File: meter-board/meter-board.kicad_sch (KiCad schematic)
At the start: 0 parts

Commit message: add title, revision
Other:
- title: (none) -> FET-PCB-meter
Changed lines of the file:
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@@
 	(generator_version "9.0")
 	(paper "A4")
+	(title_block
+		(title "FET-PCB-meter")
+		(rev "v1.0")
+	)
 	(sheet_instances
 		(path "/"

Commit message: add protection circuit
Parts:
- added D1: DF2B36FU,H3F, my_Protection:DF2B36FU,H3F, symbol my_Protection:DF2B36FU,H3F
- added D2: MM3Z12VST1G, my_Diode:MM3Z12VST1G, symbol my_Diode:MM3Z12VST1G
- added F1: 0686F0500-01, my_Fuse:0686F0500-01, symbol my_Fuse:0686F0500-01
- added J1: 2-1445053-2, my_Connector:2-1445053-2, symbol my_Connector:2-1445053-2
- added Q1: PMN100EPAX, my_Transistor:PMN100EPAX, symbol my_Transistor:PMN100EPAX
- added R1: R, my_Resistor:R_0402_1005M, symbol my_Resistor:R_0402_1005M
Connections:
- new net: F1.1, J1.1 (Pin_1)
- new net: D1.2 (A2), J1.2 (Pin_2), R1.1
- new net: D2.1 (K), Q1.4 (S)
- new net: D2.2 (A), Q1.3 (G), R1.2
- new net: D1.1 (A1), F1.2, Q1.1 (D), Q1.2 (D), Q1.5 (D), Q1.6 (D)

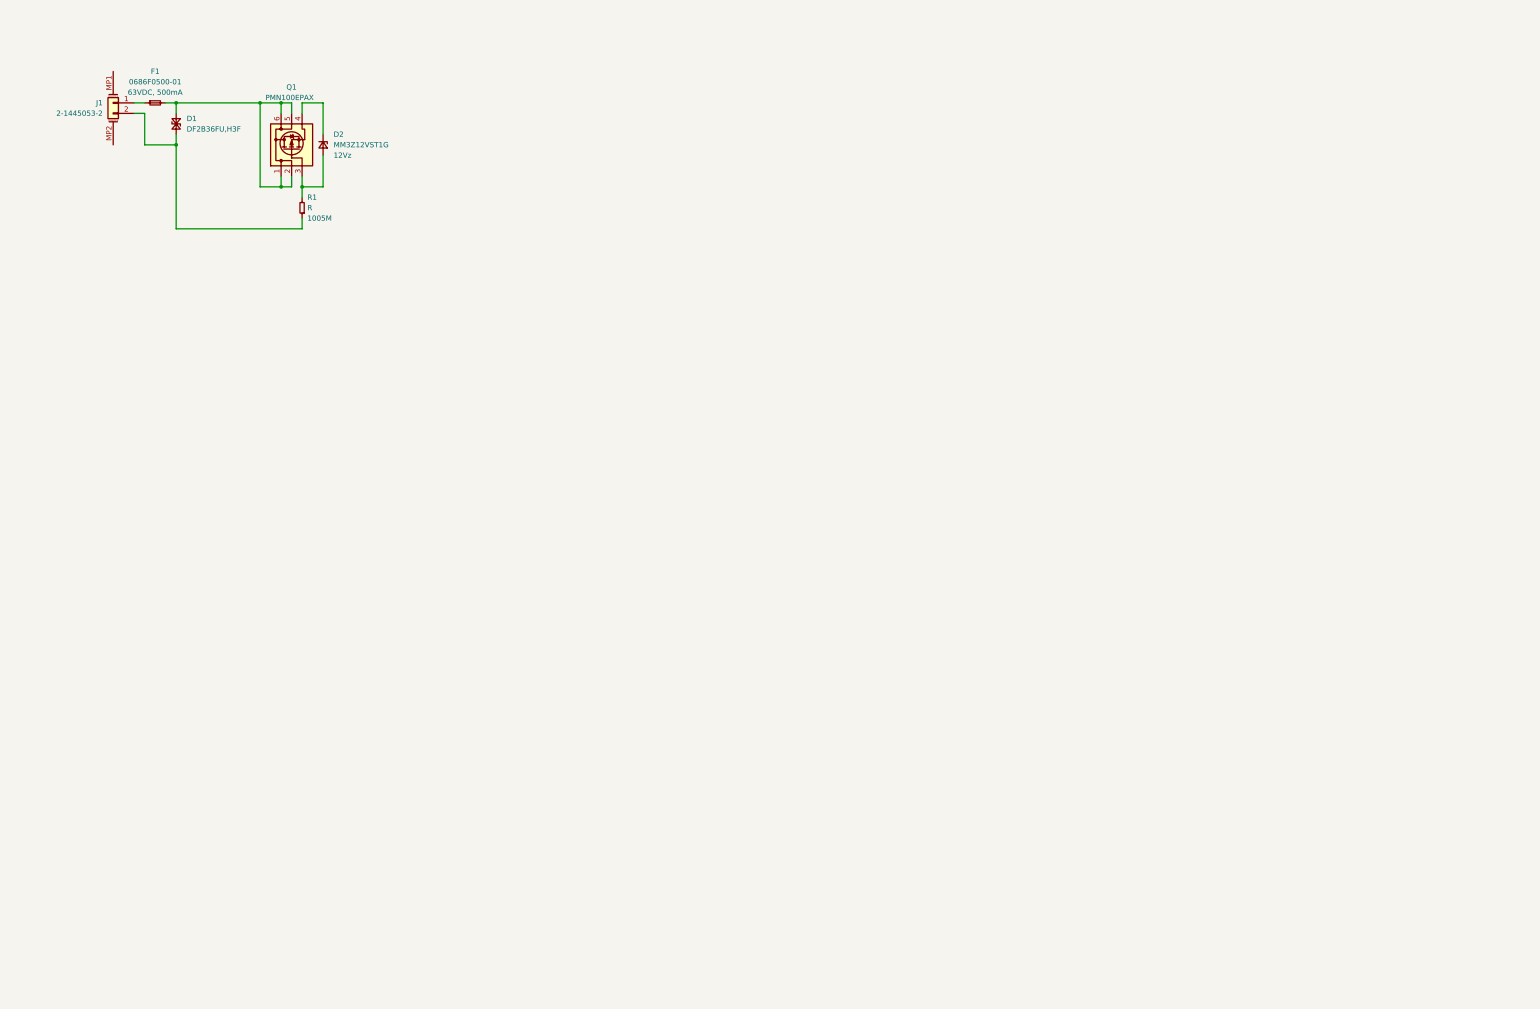
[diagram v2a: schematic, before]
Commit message: add power circuit and LEDs
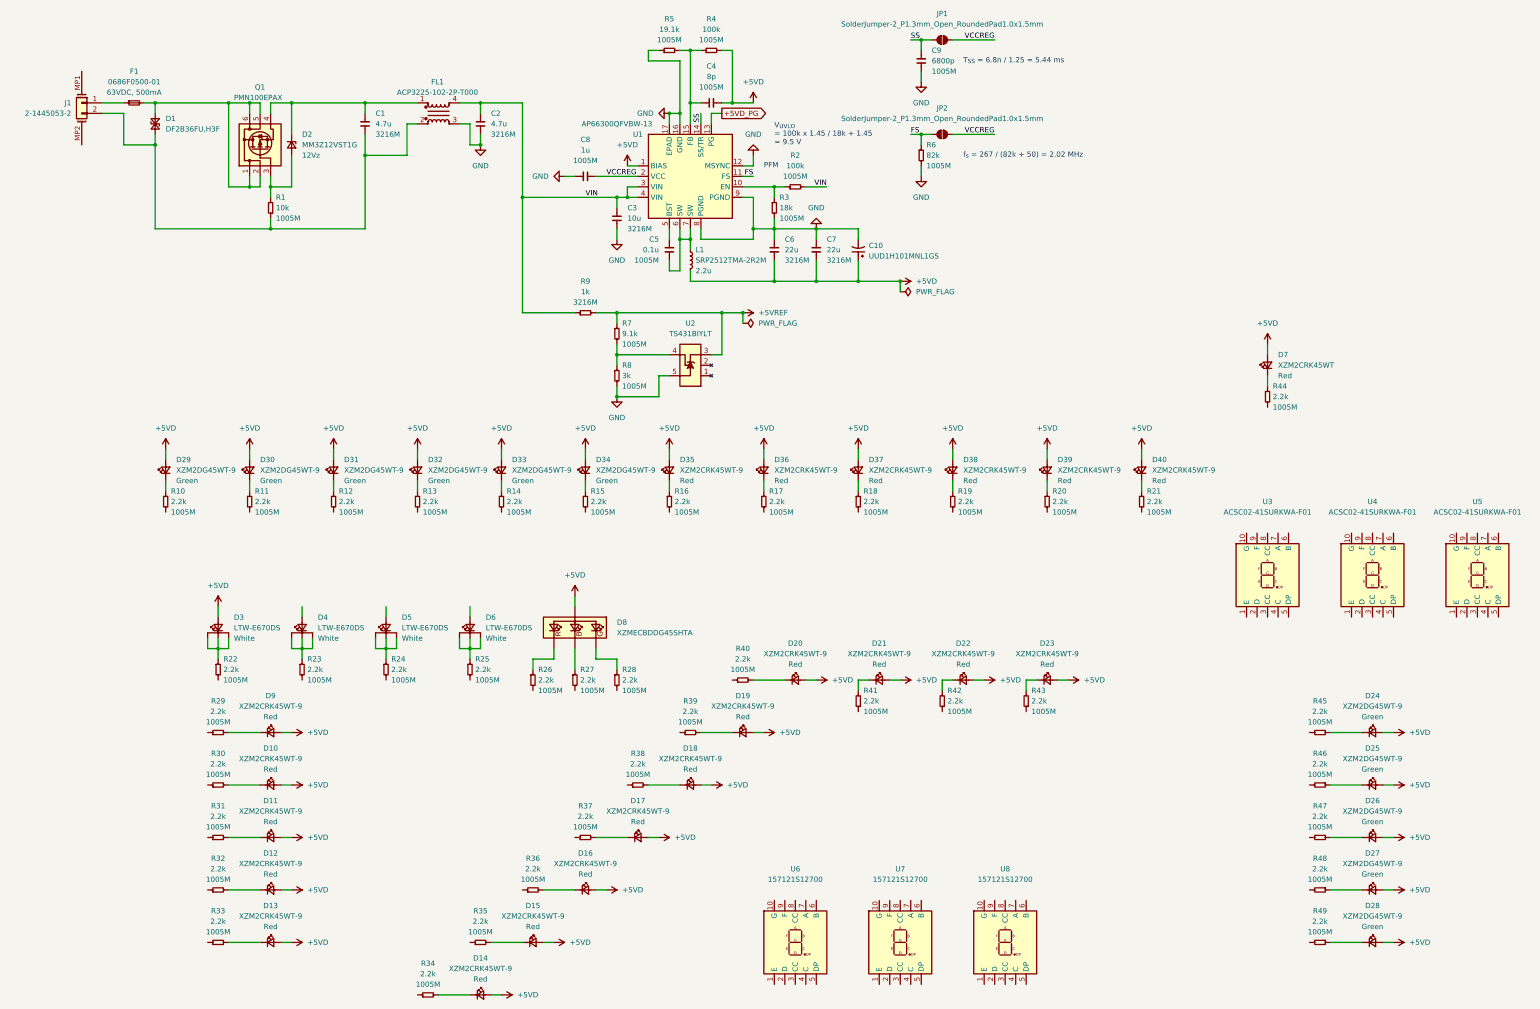
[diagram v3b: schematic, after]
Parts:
- added C1, C2: 4.7u, my_Capacitor:C_1206_3216M, symbol my_Capacitor:C_1206_3216M
- added C10: UUD1H101MNL1GS, my_Capacitor:UUD1H101MNL1GS, symbol my_Capacitor:UUD1H101MNL1GS
- added C3: 10u, my_Capacitor:C_1206_3216M, symbol my_Capacitor:C_1206_3216M
- added C4: 8p, my_Capacitor:C_0402_1005M, symbol my_Capacitor:C_0402_1005M
- added C5: 0.1u, my_Capacitor:C_0402_1005M, symbol my_Capacitor:C_0402_1005M
- added C6, C7: 22u, my_Capacitor:C_1206_3216M, symbol my_Capacitor:C_1206_3216M
- added C8: 1u, my_Capacitor:C_0402_1005M, symbol my_Capacitor:C_0402_1005M
- added C9: 6800p, my_Capacitor:C_0402_1005M, symbol my_Capacitor:C_0402_1005M
- added D10, D11, D12, D13, D14, D15, D16, D17, D18, D19, D20, D21, D22, D23, D35, D36, D37, D38, D39, D40, D9: XZM2CRK45WT-9, my_LED:XZM2CRK45WT-9, symbol my_LED:XZM2CRK45WT-9
- added D24, D25, D26, D27, D28, D29, D30, D31, D32, D33, D34: XZM2DG45WT-9, my_LED:XZM2DG45WT-9, symbol my_LED:XZM2DG45WT-9
- added D3, D4, D5, D6: LTW-E670DS, my_LED:LTW-E670DS, symbol my_LED:LTW-E670DS
- added D7: XZM2CRK45WT, my_LED:XZM2CRK45WT, symbol my_LED:XZM2CRK45WT
- added D8: XZMECBDDG45SHTA, my_LED:XZMECBDDG45SHTA, symbol my_LED:XZMECBDDG45SHTA
- added FL1: ACP3225-102-2P-T000, my_Filter:ACP3225-102-2P-T000, symbol my_Filter:ACP3225-102-2P-T000
- added JP1, JP2: SolderJumper-2_P1.3mm_Open_RoundedPad1.0x1.5mm, my_Jumper:SolderJumper-2_P1.3mm_Open_RoundedPad1.0x1.5mm, symbol my_Jumper:SolderJumper-2_P1.3mm_Open_RoundedPad1.0x1.5mm
- added L1: SRP2512TMA-2R2M, my_Inductor:SRP2512TMA-2R2M, symbol my_Inductor:SRP2512TMA-2R2M
- added R10, R11, R12, R13, R14, R15, R16, R17, R18, R19, R20, R21, R22, R23, R24, R25, R26, R27, R28, R29, R30, R31, R32, R33, R34, R35, R36, R37, R38, R39, R40, R41, R42, R43, R44, R45, R46, R47, R48, R49: 2.2k, my_Resistor:R_0402_1005M, symbol my_Resistor:R_0402_1005M
- added R2, R4: 100k, my_Resistor:R_0402_1005M, symbol my_Resistor:R_0402_1005M
- added R3: 18k, my_Resistor:R_0402_1005M, symbol my_Resistor:R_0402_1005M
- added R5: 19.1k, my_Resistor:R_0402_1005M, symbol my_Resistor:R_0402_1005M
- added R6: 82k, my_Resistor:R_0402_1005M, symbol my_Resistor:R_0402_1005M
- added R7: 9.1k, my_Resistor:R_0402_1005M, symbol my_Resistor:R_0402_1005M
- added R8: 3k, my_Resistor:R_0402_1005M, symbol my_Resistor:R_0402_1005M
- added R9: 1k, my_Resistor:R_1206_3216M, symbol my_Resistor:R_1206_3216M
- added U1: AP66300QFVBW-13, my_Regulator:AP66300QFVBW-13, symbol my_Regulator:AP66300QFVBW-13
- added U2: TS431BIYLT, my_Reference:TS431BIYLT, symbol my_Reference:TS431BIYLT
- added U3, U4, U5: ACSC02-41SURKWA-F01, my_LED:ACSC02-41SURKWA-F01, symbol my_LED:ACSC02-41SURKWA-F01
- added U6, U7, U8: 157121S12700, my_LED:157121S12700, symbol my_LED:157121S12700
- R1: value R -> 10k
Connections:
- net at D1.2 (A2), J1.2 (Pin_2), R1.1: now also C1.2, FL1.2
- net at D2.1 (K), Q1.4 (S): now also C1.1, FL1.1
- new net: D11.1 (K), R31.2
- new net: D40.1 (K), R21.1
- new net: R7.2, R8.1, U2.4 (REF)
- new net: D39.1 (K), R20.1
- new net: D24.2 (K), R45.1
- new net: C4.1, R4.1, R5.2, U1.15 (FB)
- new net: D16.1 (K), R36.2
- new net: D36.1 (K), R17.1
- new net: D8.1 (R_K), R26.1
- new net: D8.3 (B_K), R27.1
- new net: D8.4 (G_K), R28.1
- new net: D12.1 (K), R32.2
- new net: D32.2 (K), R13.1
- new net: D10.1 (K), R30.2
- new net: D15.1 (K), R35.2
- new net: D7.2 (K), R44.1
- new net: D31.2 (K), R12.1
- new net: D22.1 (K), R42.2
- new net: D33.2 (K), R14.1
- new net: D6.1 (K), D6.3 (K), D6.4 (K), R25.1
- new net: D3.1 (K), D3.3 (K), D3.4 (K), R22.1
- new net: D20.1 (K), R40.2
- new net: D19.1 (K), R39.2
- new net: D37.1 (K), R18.1
- new net: R2.1, R3.1, U1.10 (EN)
- new net: D21.1 (K), R41.2
- new net: C5.1, L1.1, U1.6 (SW), U1.7 (SW)
- new net: D27.2 (K), R48.1
- new net: D13.1 (K), R33.2
- new net: D4.1 (K), D4.3 (K), D4.4 (K), R23.1
- new net: D5.1 (K), D5.3 (K), D5.4 (K), R24.1
- new net: D26.2 (K), R47.1
- new net: D18.1 (K), R38.2
- new net: D25.2 (K), R46.1
- new net: D29.2 (K), R10.1
- new net: D14.1 (K), R34.2
- new net: D35.1 (K), R16.1
- new net: D23.1 (K), R43.2
- new net: D17.1 (K), R37.2
- new net: D28.2 (K), R49.1
- new net: D9.1 (K), R29.2
- new net: C5.2, U1.5 (BST)
- new net: D34.2 (K), R15.1
- new net: D38.1 (K), R19.1
- new net: D30.2 (K), R11.1
- new net +5VD: C10.1, C4.2, C6.2, C7.2, D10.2 (A), D11.2 (A), D12.2 (A), D13.2 (A), D14.2 (A), D15.2 (A), D16.2 (A), D17.2 (A), D18.2 (A), D19.2 (A), D20.2 (A), D21.2 (A), D22.2 (A), D23.2 (A), D24.1 (A), D25.1 (A), D26.1 (A), D27.1 (A), D28.1 (A), D29.1 (A), D3.2 (A), D30.1 (A), D31.1 (A), D32.1 (A), D33.1 (A), D34.1 (A), D35.2 (A), D36.2 (A), D37.2 (A), D38.2 (A), D39.2 (A), D40.2 (A), D7.1 (A), D8.2  (A), D9.2 (A), L1.2, R4.2, U1.1 (BIAS)
- new net +5VD_PG: U1.13 (PG)
- new net +5VREF: R7.1, R9.2, U2.3 (K)
- new net FS: JP2.1 (A), R6.1, U1.11 (FS)
- new net GND: C10.2, C2.2, C3.2, C6.1, C7.1, C8.1, C9.1, FL1.3, R3.2, R5.1, R6.2, R8.2, U1.12 (MSYNC), U1.16 (GND), U1.17 (EPAD), U1.8 (PGND), U1.9 (PGND), U2.5 (A)
- new net SS: C9.2, JP1.1 (A), U1.14 (SS/TR)
- new net VCCREG: C8.2, JP1.2 (B), JP2.2 (B), U1.2 (VCC)
- new net VIN: C2.1, C3.1, FL1.4, R2.2, R9.1, U1.3 (VIN), U1.4 (VIN)
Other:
- note added: "PFM"
- note added: "T_{SS} = 6.8n / 1.25 = 5.44 ms"
- note added: "V_{UVLO} = 100k x 1.45 / 18k + 1.45 = 9.5 V"
- note added: "f_{s} = 267 / (82k + 50) = 2.02 MHz"
- moved on the sheet: D1, D2, F1, J1, Q1, R1

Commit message: add new sheets and update circuits
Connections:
- net G6R6_R5: now reaches R20.2
- net R10_R3: now reaches R36.1
- net G6R6_R2: now reaches R17.2
- net R5_R3: now reaches R31.1
- net R5_R4: now reaches R30.1
- net R10_R2: now reaches R35.1
- net R10_R9: now reaches R42.1
- net G6R6_G5: now reaches R14.2
- net R10_R6: now reaches R39.1
- net G6R6_G3: now reaches R12.2
- net G5_G2: now reaches R48.2
- net G5_G5: now reaches R45.2
- net R10_R8: now reaches R41.1
- net G6R6_G1: now reaches R10.2
- net G5_G4: now reaches R46.2
- net G6R6_R1: now reaches R16.2
- net R10_R5: now reaches R38.1
- net R5_R5: now reaches R29.1
- net G6R6_R6: now reaches R21.2
- net G6R6_G4: now reaches R13.2
- net R10_R10: now reaches R43.1
- net G6R6_R4: now reaches R19.2
- net G6R6_G2: now reaches R11.2
- net R10_R1: now reaches R34.1
- net R10_R4: now reaches R37.1
- net R5_R2: now reaches R32.1
- net G6R6_R3: now reaches R18.2
- net R10_R7: now reaches R40.1
- net G5_G3: now reaches R47.2
- net G5_G1: now reaches R49.2
- net R5_R1: now reaches R33.1
- net G6R6_G6: now reaches R15.2
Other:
- added sheet 7seg-and-led-driver (7seg-and-led-driver.kicad_sch)
- added sheet led-meter-driver (led-meter-driver.kicad_sch)
- moved on the sheet: D7, R44

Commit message: update
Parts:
- added D41, D42, D43, D44: BAS70-04-E3-08, my_Diode:BAS70-04-E3-08, symbol my_Diode:BAS70-04-E3-08

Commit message: update circuits
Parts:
- added D45, D46, D47: BAS70-04-E3-08, my_Diode:BAS70-04-E3-08, symbol my_Diode:BAS70-04-E3-08
- added D48, D49, D50, D51, D52, D53, D54: DF2B36FU,H3F, my_Protection:DF2B36FU,H3F, symbol my_Protection:DF2B36FU,H3F
- added FB1: MMZ1005Y102CT000, my_Filter:MMZ1005Y102CT000, symbol my_Filter:MMZ1005Y102CT000
- added J2: 3-794636-8, my_Connector:3-794636-8, symbol my_Connector:3-794636-8
- added J3: 2-1445053-4, my_Connector:2-1445053-4, symbol my_Connector:2-1445053-4
- added R157, R158, R159, R160, R161, R162, R163: 100, my_Resistor:R_0402_1005M, symbol my_Resistor:R_0402_1005M
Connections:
- net +5VD: now also D4.2 (A), D5.2 (A), D6.2 (A), D45.2 (K), D46.2 (K), D47.2 (K), FB1.2
- net GND: now also D41.1 (A), D42.1 (A), D43.1 (A), D44.1 (A), D45.1 (A), D46.1 (A), D47.1 (A), D48.2 (A2), D49.2 (A2), D50.2 (A2), D51.2 (A2), D52.2 (A2), D53.2 (A2), D54.2 (A2), J2.5 (Pin_5), J2.6 (Pin_6), J2.7 (Pin_7), J2.8 (Pin_8), J3.1 (Pin_1)
- net +5VA: now reaches D43.2 (K)
- net +5VA: now also D41.2 (K), D42.2 (K), D44.2 (K), FB1.1
- net R5_AIN: now reaches D43.3 (C)
- net R5_AIN: now also D50.1 (A1), R159.2
- net R10_AIN: now reaches D44.3 (C)
- net R10_AIN: now also D51.1 (A1), R160.2
- net G5_AIN: now reaches D42.3 (C)
- net G5_AIN: now also D49.1 (A1), R158.2
- net G6R6_AIN: now reaches D41.3 (C)
- net G6R6_AIN: now also D48.1 (A1), R157.2
- new net: J3.2 (Pin_2), R161.1
- new net: J3.3 (Pin_3), R162.1
- new net: J3.4 (Pin_4), R163.1
- new net: J2.3 (Pin_3), R159.1
- new net: J2.1 (Pin_1), R157.1
- new net: J2.2 (Pin_2), R158.1
- new net: J2.4 (Pin_4), R160.1
- new net SR_CLK: D47.3 (C), D54.1 (A1), R163.2
- new net SR_MOSI: D45.3 (C), D52.1 (A1), R161.2
- new net SR_~{CS}: D46.3 (C), D53.1 (A1), R162.2
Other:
- sheet 7seg-and-led-driver ports: added 7seg_A, 7seg_B, 7seg_C, 7seg_CC1, 7seg_CC2, 7seg_CC3, 7seg_CC4, 7seg_CC5, 7seg_CC6, 7seg_D, 7seg_DP, 7seg_E, 7seg_F, 7seg_G, CLK, MOSI, RGB_B, RGB_G, RGB_R, W5_W1, W5_W2, W5_W3, W5_W4, W5_W5, ~{CS}; removed none
- moved on the sheet: C1, C10, C2, C3, C4, C5, C6, C7, C8, C9, D1, D10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

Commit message: update
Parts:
- added C23: C, my_Capacitor:C_1206_3216M, symbol my_Capacitor:C_1206_3216M
- added H1, H2, H3, H4: MountingHole_4.3mm_M4_Pad_Via, my_Mechanical:MountingHole_4.3mm_M4_Pad_Via, symbol my_Mechanical:MountingHole_4.3mm_M4_Pad_Via
- added R164: R, my_Resistor:R_1206_3216M, symbol my_Resistor:R_1206_3216M
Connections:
- net GND: now also J1.MP1 (MountPin), J1.MP2 (MountPin), J2.MP1 (MountPin), J2.MP2 (MountPin), J3.MP1 (MountPin), J3.MP2 (MountPin), C23.2, R164.2
- net W5_W3: now reaches R25.2
- net W5_W1: now reaches R22.2
- net 7seg_E: now reaches U7.1 (E)
- net 7seg_E: now also U3.1 (E), U4.1 (E), U5.1 (E), U6.1 (E), U8.1 (E)
- net 7seg_G: now reaches U7.10 (G)
- net 7seg_G: now also U3.10 (G), U4.10 (G), U5.10 (G), U6.10 (G), U8.10 (G)
- net 7seg_D: now reaches U7.2 (D)
- net 7seg_D: now also U3.2 (D), U4.2 (D), U5.2 (D), U6.2 (D), U8.2 (D)
- net 7seg_CC2: now reaches U7.3 (CC)
- net 7seg_CC2: now also U7.8 (CC)
- net 7seg_C: now reaches U7.4 (C)
- net 7seg_C: now also U3.4 (C), U4.4 (C), U5.4 (C), U6.4 (C), U8.4 (C)
- net 7seg_DP: now reaches U7.5 (DP)
- net 7seg_DP: now also U3.5 (DP), U4.5 (DP), U5.5 (DP), U6.5 (DP), U8.5 (DP)
- net 7seg_B: now reaches U7.6 (B)
- net 7seg_B: now also U3.6 (B), U4.6 (B), U5.6 (B), U6.6 (B), U8.6 (B)
- net 7seg_A: now reaches U7.7 (A)
- net 7seg_A: now also U3.7 (A), U4.7 (A), U5.7 (A), U6.7 (A), U8.7 (A)
- net 7seg_F: now reaches U7.9 (F)
- net 7seg_F: now also U3.9 (F), U4.9 (F), U5.9 (F), U6.9 (F), U8.9 (F)
- net 7seg_CC5: now reaches U4.3 (CC)
- net 7seg_CC5: now also U4.8 (CC)
- net W5_W2: now reaches R23.2
- net 7seg_CC3: now reaches U8.3 (CC)
- net 7seg_CC3: now also U8.8 (CC)
- net R1_R1: now reaches R44.2
- net W5_W4: now reaches R24.2
- net RGB_R: now reaches R26.2
- net RGB_G: now reaches R28.2
- net 7seg_CC4: now reaches U3.3 (CC)
- net 7seg_CC4: now also U3.8 (CC)
- net 7seg_CC1: now reaches U6.3 (CC)
- net 7seg_CC1: now also U6.8 (CC)
- net 7seg_CC6: now reaches U5.3 (CC)
- net 7seg_CC6: now also U5.8 (CC)
- net RGB_B: now reaches R27.2
- new net Chassis: C23.1, H1.MP, R164.1
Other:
- sheet 7seg-and-led-driver ports: added R1_R1; removed W5_W5
- moved on the sheet: D10, D11, D12, D13, D14, D15, D16, D17, D18, D19, D20, D21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

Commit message: completed designing circuit and checked DRC
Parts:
- added D55: 150060GS75003, my_LED:150060GS75003, symbol my_LED:150060GS75003
- added Q2: 2N7002K-AU_R1_000A2, my_Transistor:2N7002K-AU_R1_000A2, symbol my_Transistor:2N7002K-AU_R1_000A2
- added R165, R166: 100k, my_Resistor:R_0402_1005M, symbol my_Resistor:R_0402_1005M
- added R167: 100, my_Resistor:R_0402_1005M, symbol my_Resistor:R_0402_1005M
- C23: value C -> 1000p
- R164: value R -> 1M
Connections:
- net +5VD: now also D55.1 (A)
- net +5VD_PG: now also R167.1
- net GND: now also Q2.2 (S)
- net VCCREG: now also R166.1
- new net: Q2.1 (G), R166.2, R167.2
- new net: Q2.3 (D), R165.2
- new net: D55.2 (K), R165.1
- no-connect marks 0 -> 3
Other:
- moved on the sheet: C23, H1, R164
